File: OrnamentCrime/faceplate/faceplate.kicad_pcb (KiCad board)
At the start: 2 copper layers, 70.8 x 128.4 mm, 0 parts

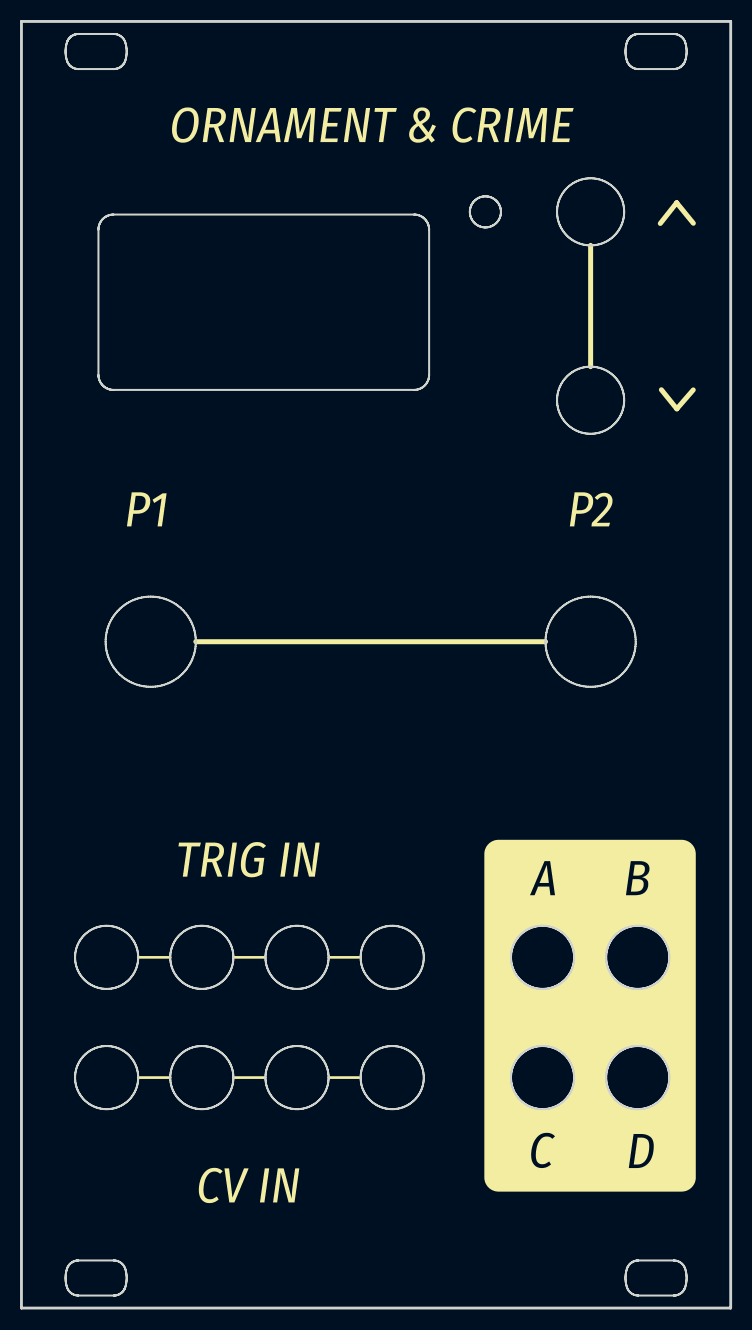
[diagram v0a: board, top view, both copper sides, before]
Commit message: Update OC faceplace
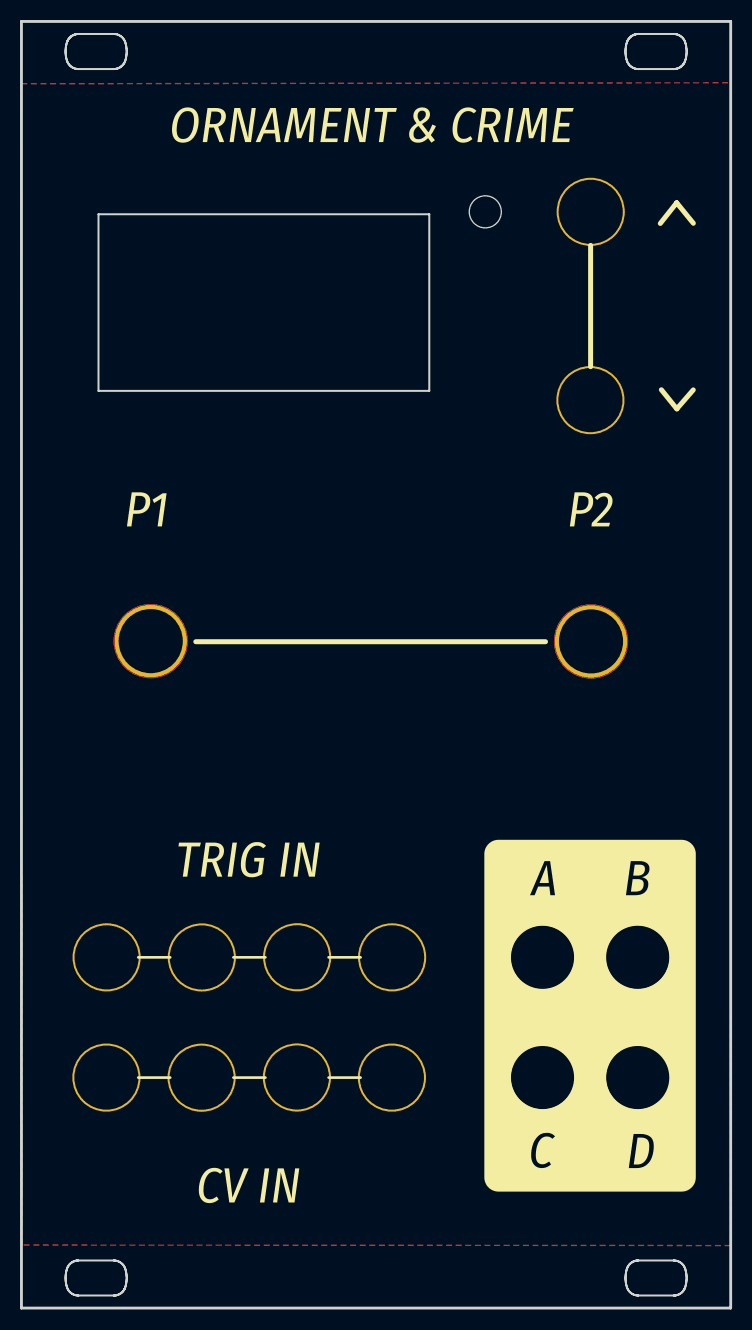
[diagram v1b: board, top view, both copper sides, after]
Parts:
- added GND: MountingHole_7.2mm_Pad_TopBottom, Library:MountingHole_7.2mm_Pad_TopBottom, F.Cu at (76.0, 88.7)
- added GND: MountingHole_7.2mm_Pad_TopBottom, Library:MountingHole_7.2mm_Pad_TopBottom, F.Cu at (119.9, 88.8)
- added REF**: MountingHole_6.4mm_M6_MiniPad_TopBottom, Library:MountingHole_6.4mm_M6_MiniPad_TopBottom, F.Cu at (81.0, 120.3)
- added REF**: MountingHole_6.4mm_M6_MiniPad_TopBottom, Library:MountingHole_6.4mm_M6_MiniPad_TopBottom, F.Cu at (119.8, 64.7)
- added REF**: MountingHole_6.4mm_M6_MiniPad_TopBottom, Library:MountingHole_6.4mm_M6_MiniPad_TopBottom, F.Cu at (119.9, 45.9)
- added REF**: MountingHole_6.4mm_M6_MiniPad_TopBottom, Library:MountingHole_6.4mm_M6_MiniPad_TopBottom, F.Cu at (115.0, 120.3)
- added REF**: MountingHole_6.4mm_M6_MiniPad_TopBottom, Library:MountingHole_6.4mm_M6_MiniPad_TopBottom, F.Cu at (81.0, 132.3)
- added REF**: MountingHole_6.4mm_M6_MiniPad_TopBottom, Library:MountingHole_6.4mm_M6_MiniPad_TopBottom, F.Cu at (90.5, 132.3)
- added REF**: MountingHole_6.4mm_M6_MiniPad_TopBottom, Library:MountingHole_6.4mm_M6_MiniPad_TopBottom, F.Cu at (124.5, 120.3)
- added REF**: MountingHole_6.4mm_M6_MiniPad_TopBottom, Library:MountingHole_6.4mm_M6_MiniPad_TopBottom, F.Cu at (100.0, 120.3)
- added REF**: MountingHole_6.4mm_M6_MiniPad_TopBottom, Library:MountingHole_6.4mm_M6_MiniPad_TopBottom, F.Cu at (124.6, 132.3)
- added REF**: MountingHole_6.4mm_M6_MiniPad_TopBottom, Library:MountingHole_6.4mm_M6_MiniPad_TopBottom, F.Cu at (100.0, 132.3)
- added REF**: MountingHole_6.4mm_M6_MiniPad_TopBottom, Library:MountingHole_6.4mm_M6_MiniPad_TopBottom, F.Cu at (71.5, 132.3)
- added REF**: MountingHole_3.2mm_M3, MountingHole:MountingHole_3.2mm_M3, F.Cu at (109.3, 45.9)
- added REF**: MountingHole_6.4mm_M6_MiniPad_TopBottom, Library:MountingHole_6.4mm_M6_MiniPad_TopBottom, F.Cu at (115.1, 132.3)
- added REF**: MountingHole_6.4mm_M6_MiniPad_TopBottom, Library:MountingHole_6.4mm_M6_MiniPad_TopBottom, F.Cu at (90.6, 120.3)
- added REF**: MountingHole_6.4mm_M6_MiniPad_TopBottom, Library:MountingHole_6.4mm_M6_MiniPad_TopBottom, F.Cu at (71.5, 120.3)
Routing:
- added copper zone on F.Cu, net (none)
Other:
- outline, holes or cut-outs redrawn
